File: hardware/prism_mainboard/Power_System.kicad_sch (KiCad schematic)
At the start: 0 parts

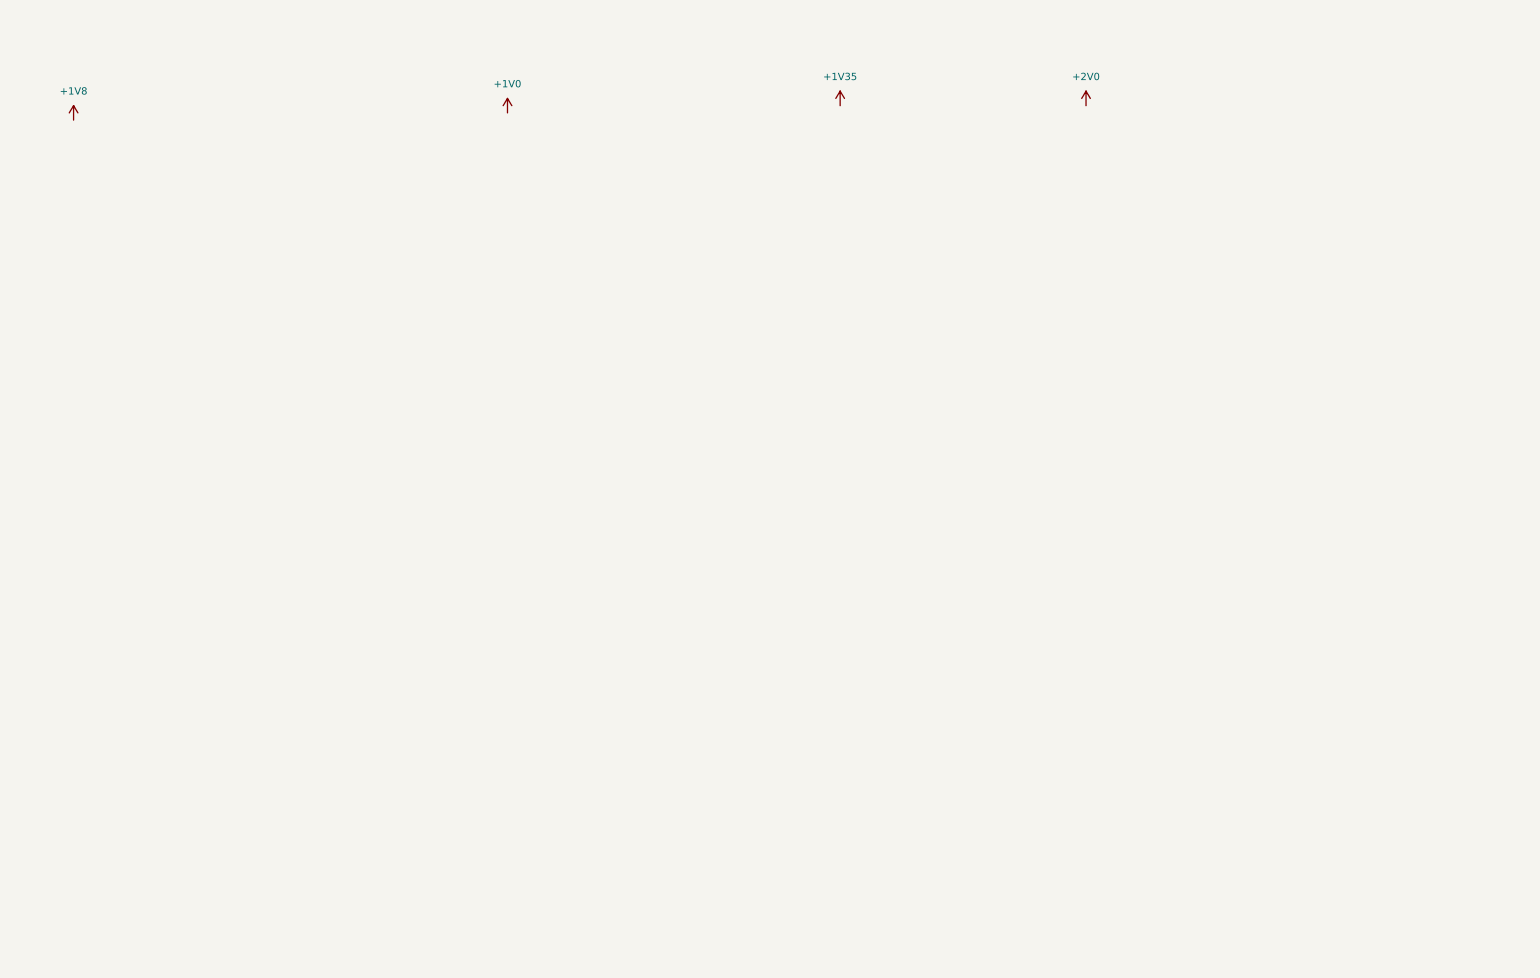
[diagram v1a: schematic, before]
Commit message: Schematic Updates
Updated the DDR3 DRAM to 4Gb, added a lot of nets and started updating the power and decoupling components. Updated .gitignore to avoid .mkv files.
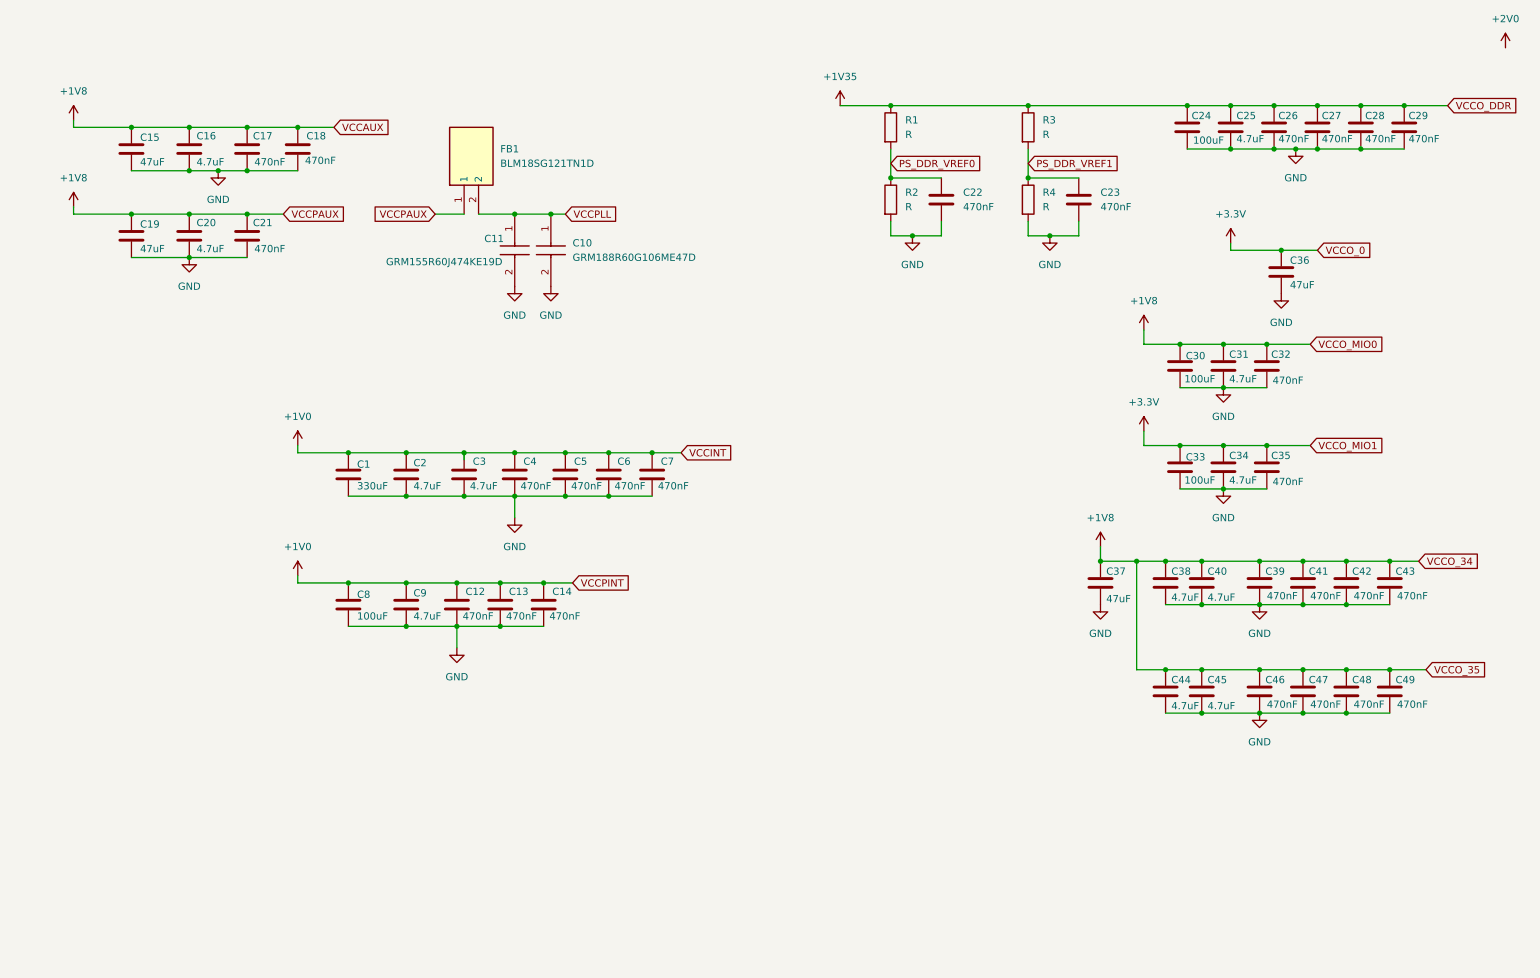
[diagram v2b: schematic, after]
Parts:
- added C1: 330uF, symbol Device:C
- added C10: GRM188R60G106ME47D, CAPC1608X90N, symbol SamacSys:GRM188R60G106ME47D
- added C11: GRM155R60J474KE19D, CAPC1005X70N, symbol SamacSys:GRM155R60J474KE19D
- added C12, C13, C14, C17, C18, C21, C22, C23, C26, C27, C28, C29, C32, C35, C39, C4, C41, C42, C43, C46, C47, C48, C49, C5, C6, C7: 470nF, symbol Device:C
- added C15, C19, C36, C37: 47uF, symbol Device:C
- added C16, C2, C20, C25, C3, C31, C34, C38, C40, C44, C45, C9: 4.7uF, symbol Device:C
- added C24, C30, C33, C8: 100uF, symbol Device:C
- added FB1: BLM18SG121TN1D, BLM18EG101TH1D, symbol SamacSys:BLM18SG121TN1D
- added R1, R2, R3, R4: R, symbol Device:R
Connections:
- net +1V0: now also C1.1, C12.1, C13.1, C14.1, C2.1, C3.1, C4.1, C5.1, C6.1, C7.1, C8.1, C9.1
- net +1V35: now also C24.1, C25.1, C26.1, C27.1, C28.1, C29.1, R1.1, R3.1
- net +1V8: now also C15.1, C16.1, C17.1, C18.1, C19.1, C20.1, C21.1, C30.1, C31.1, C32.1, C37.1, C38.1, C39.1, C40.1, C41.1, C42.1, C43.1, C44.1, C45.1, C46.1, C47.1, C48.1, C49.1, FB1.1
- new net +3.3V: C33.1, C34.1, C35.1, C36.1
- new net GND: C1.2, C10.2, C11.2, C12.2, C13.2, C14.2, C15.2, C16.2, C17.2, C18.2, C19.2, C2.2, C20.2, C21.2, C22.2, C23.2, C24.2, C25.2, C26.2, C27.2, C28.2, C29.2, C3.2, C30.2, C31.2, C32.2, C33.2, C34.2, C35.2, C36.2, C37.2, C38.2, C39.2, C4.2, C40.2, C41.2, C42.2, C43.2, C44.2, C45.2, C46.2, C47.2, C48.2, C49.2, C5.2, C6.2, C7.2, C8.2, C9.2, R2.2, R4.2
- new net PS_DDR_VREF0: C22.1, R1.2, R2.1
- new net PS_DDR_VREF1: C23.1, R3.2, R4.1
- new net VCCPLL: C10.1, C11.1, FB1.2

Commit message: Schematic Updates
Updated schematics. Most of the power and decoupling is set for most if not all devices. Need to interconnect devices. Still reading datasheets
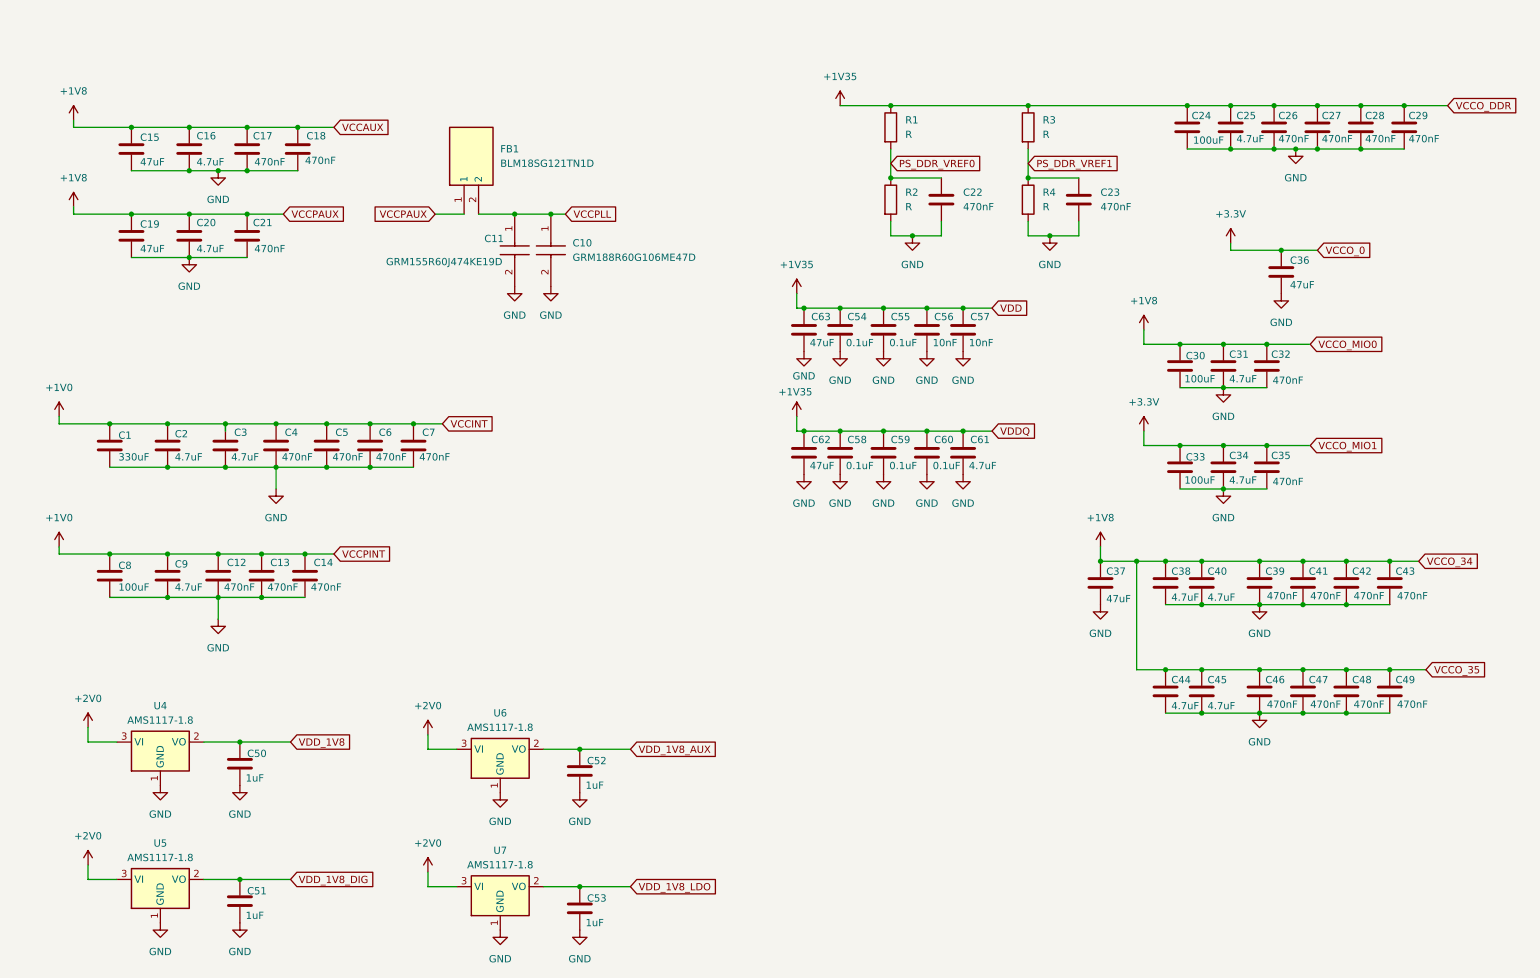
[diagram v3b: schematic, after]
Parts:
- added C50, C51, C52, C53: 1uF, Capacitor_SMD:C_0805_2012Metric_Pad1.18x1.45mm_HandSolder, symbol Device:C
- added C54, C55, C58, C59, C60: 0.1uF, Capacitor_SMD:C_0402_1005Metric, symbol Device:C
- added C56: 10nF, Capacitor_SMD:C_0402_1005Metric, symbol Device:C
- added C57: 10nF, Capacitor_SMD:C_0402_1005Metric_Pad0.74x0.62mm_HandSolder, symbol Device:C
- added C61: 4.7uF, Capacitor_SMD:C_0402_1005Metric_Pad0.74x0.62mm_HandSolder, symbol Device:C
- added C62, C63: 47uF, Capacitor_SMD:C_0805_2012Metric_Pad1.18x1.45mm_HandSolder, symbol Device:C
- added U4, U5, U6, U7: AMS1117-1.8, Package_TO_SOT_SMD:SOT-223-3_TabPin2, symbol Regulator_Linear:AMS1117-1.8
- C12, C13, C14, C17, C18, C21, C22, C23, C26, C27, C28, C29, C32, C35, C39, C4, C41, C42, C43, C46, C47, C48, C49, C5, C6, C7: footprint (none) -> Capacitor_SMD:C_0402_1005Metric_Pad0.74x0.62mm_HandSolder
- C15, C16, C19, C2, C20, C24, C25, C3, C30, C31, C33, C34, C36, C37, C38, C40, C44, C45, C8, C9: footprint (none) -> Capacitor_SMD:C_0805_2012Metric_Pad1.18x1.45mm_HandSolder
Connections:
- net +1V35: now also C54.1, C55.1, C56.1, C57.1, C58.1, C59.1, C60.1, C61.1, C62.1, C63.1
- net +2V0: now also U4.3 (VI), U5.3 (VI), U6.3 (VI), U7.3 (VI)
- net GND: now also C50.2, C51.2, C52.2, C53.2, C54.2, C55.2, C56.2, C57.2, C58.2, C59.2, C60.2, C61.2, C62.2, C63.2, U4.1 (GND), U5.1 (GND), U6.1 (GND), U7.1 (GND)
- new net VDD_1V8: C50.1, U4.2 (VO)
- new net VDD_1V8_AUX: C52.1, U6.2 (VO)
- new net VDD_1V8_DIG: C51.1, U5.2 (VO)
- new net VDD_1V8_LDO: C53.1, U7.2 (VO)
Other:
- moved on the sheet: C1, C12, C13, C14, C2, C3, C4, C5, C6, C7, C8, C9

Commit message: Updates
Mostly Schematic updates, nothing too big. Added a few datasheets
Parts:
- removed C1: 330uF, symbol Device:C
- added C1: T494D337K010AT, T494D, symbol SamacSys:T494D337K010AT
- R1, R2, R3, R4: footprint (none) -> Resistor_SMD:R_0805_2012Metric_Pad1.20x1.40mm_HandSolder
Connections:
- net +1V0: now also C1.1 (+)
- net GND: now also C1.2 (-)
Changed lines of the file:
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@@
 	(wire
 		(pts
-			(xy 171.45 48.26) (xy 171.45 50.8)
+			(xy 38.1 96.52) (xy 38.1 91.44)
 		)
 		(stroke
@@
 	(wire
 		(pts
-			(xy 48.26 39.37) (xy 53.34 39.37)
+			(xy 171.45 48.26) (xy 171.45 50.8)
 		)
 		(stroke
@@
 	(wire
 		(pts
-			(xy 30.48 163.83) (xy 35.56 163.83)
+			(xy 48.26 39.37) (xy 53.34 39.37)
 		)
 		(stroke
@@
 	(wire
 		(pts
-			(xy 229.87 69.85) (xy 237.49 69.85)
+			(xy 30.48 163.83) (xy 35.56 163.83)
 		)
 		(stroke
@@
 	(wire
 		(pts
-			(xy 58.42 39.37) (xy 67.31 39.37)
+			(xy 229.87 69.85) (xy 237.49 69.85)
 		)
 		(stroke
@@
 	(wire
 		(pts
-			(xy 251.46 115.57) (xy 259.08 115.57)
+			(xy 58.42 39.37) (xy 67.31 39.37)
 		)
 		(stroke
@@
 	(wire
 		(pts
-			(xy 34.29 91.44) (xy 44.45 91.44)
+			(xy 251.46 115.57) (xy 259.08 115.57)
 		)
 		(stroke
@@
 	(wire
 		(pts
+			(xy 38.1 91.44) (xy 44.45 91.44)
+		)
+		(stroke
+			(width 0)
+			(type default)
+		)
+	)
+	(wire
+		(pts
 			(xy 195.58 40.64) (xy 204.47 40.64)
 		)
@@
 	(wire
 		(pts
+			(xy 34.29 96.52) (xy 38.1 96.52)
+		)
+		(stroke
+			(width 0)
+			(type default)
+		)
+	)
+	(wire
+		(pts
 			(xy 116.84 140.97) (xy 125.73 140.97)
 		)
@@
 			)
 		)
-		(property "Footprint" ""
+		(property "Footprint" "Resistor_SMD:R_0805_2012Metric_Pad1.20x1.40mm_HandSolder"
 			(at 193.802 44.45 90)
 			(hide yes)
@@
 			)
 		)
-		(property "Footprint" ""
+		(property "Footprint" "Resistor_SMD:R_0805_2012Metric_Pad1.20x1.40mm_HandSolder"
 			(at 193.802 31.75 90)
 			(hide yes)
@@
 			)
 		)
-		(property "Footprint" ""
+		(property "Footprint" "Resistor_SMD:R_0805_2012Metric_Pad1.20x1.40mm_HandSolder"
 			(at 169.672 44.45 90)
 			(hide yes)
@@
 			)
 		)
-		(property "Footprint" ""
+		(property "Footprint" "Resistor_SMD:R_0805_2012Metric_Pad1.20x1.40mm_HandSolder"
 			(at 169.672 31.75 90)
 			(hide yes)
@@
 	)
 	(symbol
+		(lib_id "SamacSys:T494D337K010AT")
+		(at 34.29 83.82 270)
+		(unit 1)
+		(body_style 1)
+		(exclude_from_sim no)
+		(in_bom yes)
+		(on_board yes)
+		(in_pos_files yes)
+		(dnp no)
+		(property "Reference" "C1"
+			(at 31.242 87.63 90)
+			(show_name no)
+			(do_not_autoplace no)
+			(effects
+				(font
+					(size 1.27 1.27)
+				)
+				(justify left)
+			)
+		)
+		(property "Value" "T494D337K010AT"
+			(at 17.018 92.964 90)
+			(show_name no)
+			(do_not_autoplace no)
+			(effects
+				(font
+					(size 1.27 1.27)
+				)
+				(justify left)
+			)
+		)
+		(property "Footprint" "T494D"
+			(at -61.9 92.71 0)
+			(hide yes)
+			(show_name no)
+			(do_not_autoplace no)
+			(effects
+				(font
+					(size 1.27 1.27)
+				)
+				(justify left top)
+			)
+		)
+		(property "Datasheet" "https://www.yageogroup.com/content/datasheet/asset/file/KEM_T2008_T494"
+			(at -161.9 92.71 0)
+			(hide yes)
+			(show_name no)
+			(do_not_autoplace no)
+			(effects
+				(font
+					(size 1.27 1.27)
+				)
+				(justify left top)
+			)
+		)
+		(property "Description" "SMD, MnO2, Molded, Low ESR"
+			(at 34.29 83.82 0)
+			(hide yes)
+			(show_name no)
+			(do_not_autoplace no)
+			(effects
+				(font
+					(size 1.27 1.27)
+				)
+			)
+		)
+		(property "Height" "3.1"
+			(at -361.9 92.71 0)
+			(hide yes)
+			(show_name no)
+			(do_not_autoplace no)
+			(effects
+				(font
+					(size 1.27 1.27)
+				)
+				(justify left top)
+			)
+		)
+		(property "Manufacturer_Name" "Yageo Group"
+			(at -461.9 92.71 0)
+			(hide yes)
+			(show_name no)
+			(do_not_autoplace no)
+			(effects
+				(font
+					(size 1.27 1.27)
+				)
+				(justify left top)
+			)
+		)
+		(property "Manufacturer_Part_Number" "T494D337K010AT"
+			(at -561.9 92.71 0)
+			(hide yes)
+			(show_name no)
+			(do_not_autoplace no)
+			(effects
+				(font
+					(size 1.27 1.27)
+				)
+				(justify left top)
+			)
+		)
+		(property "Mouser Part Number" "80-T494D337K010AT"
+			(at -661.9 92.71 0)
+			(hide yes)
+			(show_name no)
+			(do_not_autoplace no)
+			(effects
+				(font
+					(size 1.27 1.27)
+				)
+				(justify left top)
+			)
+		)
+		(property "Mouser Price/Stock" "https://www.mouser.co.uk/ProductDetail/KEMET/T494D337K010AT?qs=AaRlLUpeMszja%252B890bVUVg%3D%3D"
+			(at -761.9 92.71 0)
+			(hide yes)
+			(show_name no)
+			(do_not_autoplace no)
+			(effects
+				(font
+					(size 1.27 1.27)
+				)
+				(justify left top)
+			)
+		)
+		(property "Arrow Part Number" "T494D337K010AT"
+			(at -861.9 92.71 0)
+			(hide yes)
+			(show_name no)
+			(do_not_autoplace no)
+			(effects
+				(font
+					(size 1.27 1.27)
+				)
+				(justify left top)
+			)
+		)
+		(property "Arrow Price/Stock" "https://www.arrow.com/en/products/t494d337k010at/kemet-corporation"
+			(at -961.9 92.71 0)
+			(hide yes)
+			(show_name no)
+			(do_not_autoplace no)
+			(effects
+				(font
+					(size 1.27 1.27)
+				)
+				(justify left top)
+			)
+		)
+		(pin "1"
+		)
+		(pin "2"
+		)
+		(instances
+			(project "prism_mainboard"
+				(path "/1d5f25f9-3e6f-41df-a8ec-41fc885bea9a/2fdb70e6-73b6-44a0-9464-64831d844f2c"
+					(reference "C1")
+					(unit 1)
+				)
+			)
+		)
+	)
+	(symbol
 		(lib_id "power:GND")
 		(at 53.34 118.11 0)
@@
 					(unit 1)
 				)
-			)
-		)
-	)
-	(symbol
-		(lib_id "Device:C")
-		(at 34.29 87.63 0)
-		(unit 1)
-		(body_style 1)
-		(exclude_from_sim no)
-		(in_bom yes)
-		(on_board yes)
-		(in_pos_files yes)
-		(dnp no)
-		(property "Reference" "C1"
-			(at 35.814 85.852 0)
-			(show_name no)
-			(do_not_autoplace no)
-			(effects
-				(font
-					(size 1.27 1.27)
-				)
-				(justify left)
-			)
-		)
-		(property "Value" "330uF"
-			(at 35.814 89.662 0)
-			(show_name no)
-			(do_not_autoplace no)
-			(effects
-				(font
-					(size 1.27 1.27)
-				)
-				(justify left)
-			)
-		)
-		(property "Footprint" ""
-			(at 35.2552 91.44 0)
-			(hide yes)
-			(show_name no)
-			(do_not_autoplace no)
-			(effects
-				(font
-					(size 1.27 1.27)
-				)
-			)
-		)
-		(property "Datasheet" ""
-			(at 34.29 87.63 0)
-			(hide yes)
-			(show_name no)
-			(do_not_autoplace no)
-			(effects
-				(font
-					(size 1.27 1.27)
-				)
-			)
-		)
-		(property "Description" "Unpolarized capacitor"
-			(at 34.29 87.63 0)
-			(hide yes)
-			(show_name no)
-			(do_not_autoplace no)
-			(effects
-				(font
-					(size 1.27 1.27)
-				)
-			)
-		)
-		(pin "1"
-		)
-		(pin "2"
-		)
-		(instances
-			(project "prism_mainboard"
-				(path "/1d5f25f9-3e6f-41df-a8ec-41fc885bea9a/2fdb70e6-73b6-44a0-9464-64831d844f2c"
-					(reference "C1")
-					(unit 1)
-				)
